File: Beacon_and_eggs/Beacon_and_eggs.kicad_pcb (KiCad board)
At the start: 4 copper layers, 40 x 70 mm, 71 parts, among them J1 USB_C_Receptacle_USB2.0_16P, J2 Conn_01x03_Pin, J3 Conn_01x02_Pin, Q1 NTA4151P, Q2 NTA4153N, SW3 RESET, SW4 BOOT0, U1 SA818V, U2 STM32F411CEUx, U3 ADXL343, U4 MIC5528-3.3YMX-TR, U6 BQ24070RHLR, Y1 25MHz 18pF, Y2 32.768kHz 12.5pF

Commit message: added missing via net labels
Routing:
- net GND: vias 44 -> 61
- net (no net): vias 17 -> 1
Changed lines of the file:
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@@
 	)
 	(via
-		(at 133 62)
-		(size 0.6)
-		(drill 0.3)
-		(layers "F.Cu" "B.Cu")
-		(net 0)
-	)
-	(via
-		(at 131 60)
-		(size 0.6)
-		(drill 0.3)
-		(layers "F.Cu" "B.Cu")
-		(net 0)
-	)
-	(via
-		(at 138 67)
-		(size 0.6)
-		(drill 0.3)
-		(layers "F.Cu" "B.Cu")
-		(net 0)
-	)
-	(via
-		(at 130 59)
-		(size 0.6)
-		(drill 0.3)
-		(layers "F.Cu" "B.Cu")
-		(net 0)
-	)
-	(via
-		(at 137 66)
-		(size 0.6)
-		(drill 0.3)
-		(layers "F.Cu" "B.Cu")
-		(net 0)
-	)
-	(via
-		(at 134 63)
-		(size 0.6)
-		(drill 0.3)
-		(layers "F.Cu" "B.Cu")
-		(net 0)
-	)
-	(via
-		(at 130 63)
-		(size 0.6)
-		(drill 0.3)
-		(layers "F.Cu" "B.Cu")
-		(net 0)
-	)
-	(via
-		(at 129 58)
-		(size 0.6)
-		(drill 0.3)
-		(layers "F.Cu" "B.Cu")
-		(net 0)
-	)
-	(via
-		(at 132 61)
-		(size 0.6)
-		(drill 0.3)
-		(layers "F.Cu" "B.Cu")
-		(net 0)
-	)
-	(via
-		(at 136 65)
-		(size 0.6)
-		(drill 0.3)
-		(layers "F.Cu" "B.Cu")
-		(net 0)
-	)
-	(via
-		(at 135 68)
-		(size 0.6)
-		(drill 0.3)
-		(layers "F.Cu" "B.Cu")
-		(net 0)
-	)
-	(via
-		(at 128 61)
-		(size 0.6)
-		(drill 0.3)
-		(layers "F.Cu" "B.Cu")
-		(net 0)
-	)
-	(via
-		(at 127 60)
-		(size 0.6)
-		(drill 0.3)
-		(layers "F.Cu" "B.Cu")
-		(net 0)
-	)
-	(via
-		(at 131 64)
-		(size 0.6)
-		(drill 0.3)
-		(layers "F.Cu" "B.Cu")
-		(net 0)
-	)
-	(via
-		(at 136 69)
-		(size 0.6)
-		(drill 0.3)
-		(layers "F.Cu" "B.Cu")
-		(net 0)
-	)
-	(via
-		(at 129 62)
-		(size 0.6)
-		(drill 0.3)
-		(layers "F.Cu" "B.Cu")
-		(net 0)
-	)
-	(via
-		(at 132 65)
+		(at 137.668 70.104)
 		(size 0.6)
 		(drill 0.3)
@@
 	)
 	(via
+		(at 133 62)
+		(size 0.6)
+		(drill 0.3)
+		(layers "F.Cu" "B.Cu")
+		(free yes)
+		(net 2)
+	)
+	(via
 		(at 153.5275 65.6075)
 		(size 0.6)
@@
 	)
 	(via
+		(at 131 60)
+		(size 0.6)
+		(drill 0.3)
+		(layers "F.Cu" "B.Cu")
+		(free yes)
+		(net 2)
+	)
+	(via
+		(at 138 67)
+		(size 0.6)
+		(drill 0.3)
+		(layers "F.Cu" "B.Cu")
+		(free yes)
+		(net 2)
+	)
+	(via
+		(at 130 59)
+		(size 0.6)
+		(drill 0.3)
+		(layers "F.Cu" "B.Cu")
+		(free yes)
+		(net 2)
+	)
+	(via
+		(at 137 66)
+		(size 0.6)
+		(drill 0.3)
+		(layers "F.Cu" "B.Cu")
+		(free yes)
+		(net 2)
+	)
+	(via
 		(at 151.8475 84)
 		(size 0.6)
@@
 	)
 	(via
+		(at 134 63)
+		(size 0.6)
+		(drill 0.3)
+		(layers "F.Cu" "B.Cu")
+		(free yes)
+		(net 2)
+	)
+	(via
 		(at 144.6 72.8)
 		(size 0.6)
@@
 	)
 	(via
+		(at 130 63)
+		(size 0.6)
+		(drill 0.3)
+		(layers "F.Cu" "B.Cu")
+		(free yes)
+		(net 2)
+	)
+	(via
+		(at 129 58)
+		(size 0.6)
+		(drill 0.3)
+		(layers "F.Cu" "B.Cu")
+		(free yes)
+		(net 2)
+	)
+	(via
 		(at 150.4025 70.3325)
 		(size 0.6)
@@
 	)
 	(via
+		(at 132 61)
+		(size 0.6)
+		(drill 0.3)
+		(layers "F.Cu" "B.Cu")
+		(free yes)
+		(net 2)
+	)
+	(via
 		(at 149.8 59.8)
 		(size 0.6)
@@
 	)
 	(via
+		(at 136 65)
+		(size 0.6)
+		(drill 0.3)
+		(layers "F.Cu" "B.Cu")
+		(free yes)
+		(net 2)
+	)
+	(via
 		(at 135.6 104.7)
 		(size 0.6)
@@
 	)
 	(via
+		(at 135 68)
+		(size 0.6)
+		(drill 0.3)
+		(layers "F.Cu" "B.Cu")
+		(free yes)
+		(net 2)
+	)
+	(via
 		(at 130.16 106.8)
 		(size 0.6)
@@
 	)
 	(via
+		(at 128 61)
+		(size 0.6)
+		(drill 0.3)
+		(layers "F.Cu" "B.Cu")
+		(free yes)
+		(net 2)
+	)
+	(via
 		(at 143.5675 97.16)
 		(size 0.6)
@@
 	)
 	(via
+		(at 127 60)
+		(size 0.6)
+		(drill 0.3)
+		(layers "F.Cu" "B.Cu")
+		(free yes)
+		(net 2)
+	)
+	(via
 		(at 140.07 108.47)
 		(size 0.6)
@@
 	)
 	(via
+		(at 131 64)
+		(size 0.6)
+		(drill 0.3)
+		(layers "F.Cu" "B.Cu")
+		(free yes)
+		(net 2)
+	)
+	(via
 		(at 122.5 60.75)
 		(size 0.6)
@@
 	)
 	(via
+		(at 136 69)
+		(size 0.6)
+		(drill 0.3)
+		(layers "F.Cu" "B.Cu")
+		(free yes)
+		(net 2)
+	)
+	(via
+		(at 129 62)
+		(size 0.6)
+		(drill 0.3)
+		(layers "F.Cu" "B.Cu")
+		(free yes)
+		(net 2)
+	)
+	(via
+		(at 132 65)
+		(size 0.6)
+		(drill 0.3)
+		(layers "F.Cu" "B.Cu")
+		(free yes)
+		(net 2)
+	)
+	(via
 		(at 146.349661 99.3225)
 		(size 0.6)
@@
 		(start 137.5706 68.525)
 		(end 140.225 68.525)
-		(width 0.2)
+		(width 0.3)
 		(layer "F.Cu")
 		(net 63)
@@
 		(start 125.0372 56)
 		(end 137.5664 68.5292)
-		(width 0.2)
+		(width 0.3)
 		(layer "B.Cu")
 		(net 63)
@@
 		(min_thickness 0.25)
 		(filled_areas_thickness no)
-		(fill yes
+		(fill
 			(thermal_gap 0.5)
 			(thermal_bridge_width 0.5)
@@
 		(min_thickness 0.25)
 		(filled_areas_thickness no)
-		(fill yes
+		(fill
 			(thermal_gap 0.5)
 			(thermal_bridge_width 0.5)
@@
 		(min_thickness 0.25)
 		(filled_areas_thickness no)
-		(fill yes
+		(fill
 			(thermal_gap 0.5)
 			(thermal_bridge_width 0.5)
@@
 		(min_thickness 0.25)
 		(filled_areas_thickness no)
-		(fill yes
+		(fill
 			(thermal_gap 0.5)
 			(thermal_bridge_width 0.5)
@@
 		(min_thickness 0.25)
 		(filled_areas_thickness no)
-		(fill yes
+		(fill
 			(thermal_gap 0.5)
 			(thermal_bridge_width 0.5)
@@
 		(min_thickness 0.25)
 		(filled_areas_thickness no)
-		(fill yes
+		(fill
 			(thermal_gap 0.5)
 			(thermal_bridge_width 0.5)

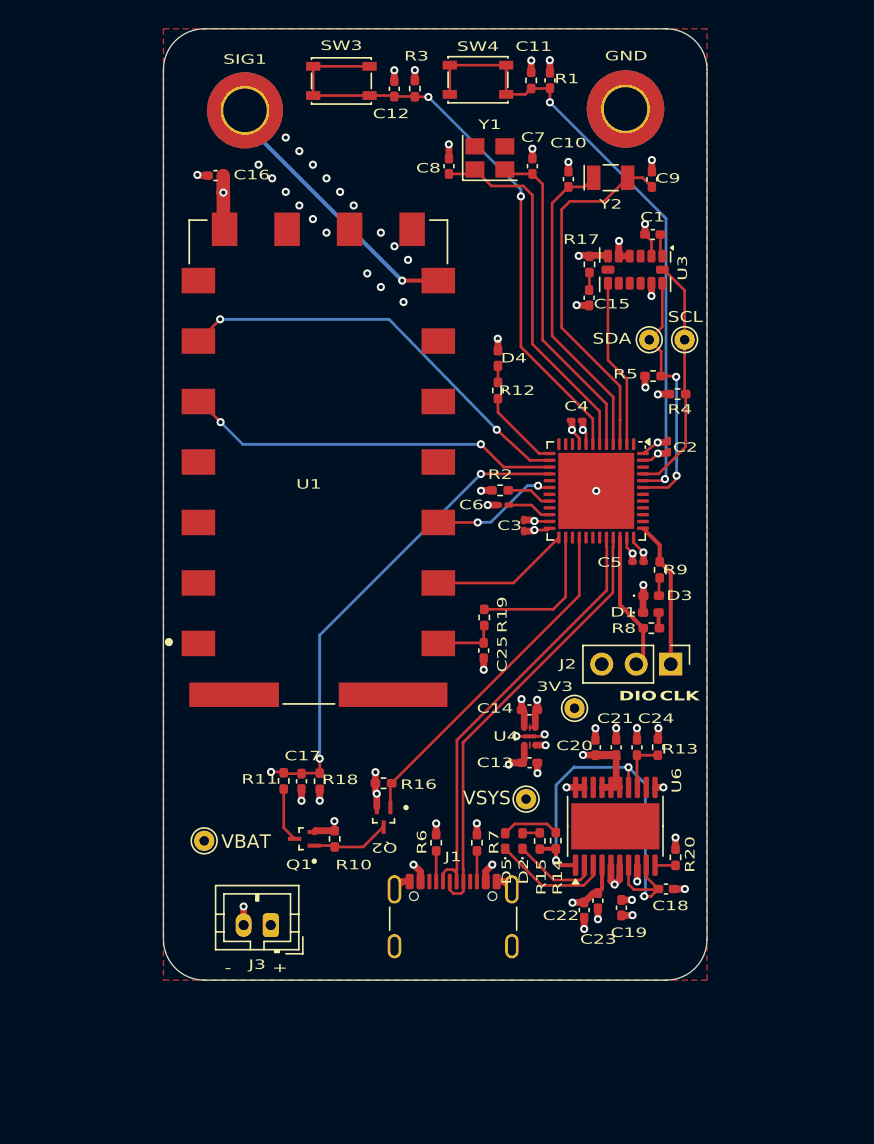
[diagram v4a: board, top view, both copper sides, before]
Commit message: Added complete BOM, replaced a footprint, added missing STEP files
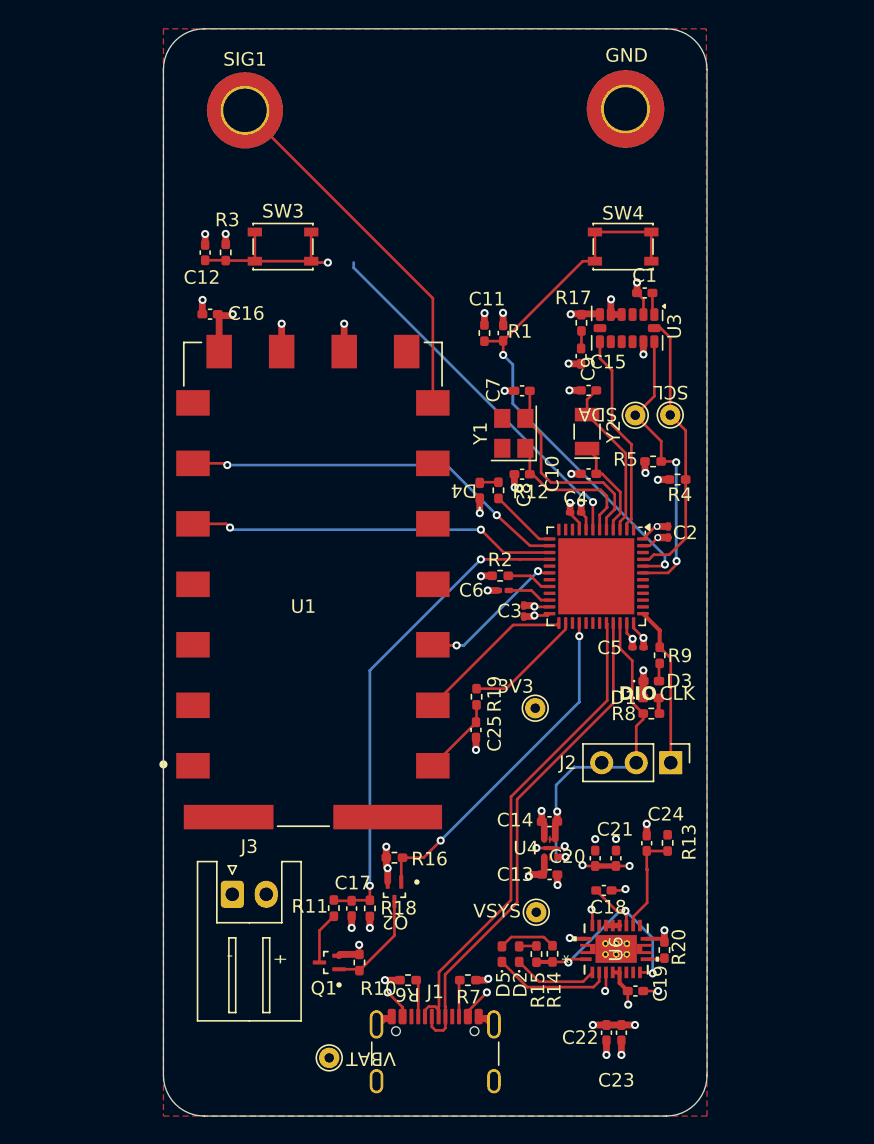
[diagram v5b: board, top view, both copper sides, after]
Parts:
- C1: value 0.1F -> 0.1uF
- C11, C12: value 0.1uf -> 0.1uF
- J3: footprint Connector_JST:JST_PH_B2B-PH-K_1x02_P2.00mm_Vertical -> Connector_JST:JST_XH_S2B-XH-A_1x02_P2.50mm_Horizontal
- U1: value SA818V -> SA868S
- U2: value STM32F411CEUx -> STM32F411CEU6TR
- U6: footprint Package_SO:HTSSOP-20-1EP_4.4x6.5mm_P0.65mm_EP3.4x6.5mm_Mask2.4x3.7mm -> BQ24070RHLR:RHL20_2P05X3P05
- moved C8 23.3 mm to (146.4, 82.8), turned to 0 degrees
- moved C10 21.7 mm to (151.3, 82.7), turned to 0 degrees
- moved Y1 20.3 mm to (145.8, 79.8), turned to 90 degrees
- moved C11 18.9 mm to (145.0, 72.4)
- moved R1 18.9 mm to (143.6, 72.4)
- moved Y2 18.8 mm to (151.2, 79.6), turned to 90 degrees
- moved TP5 18.4 mm to (132.2, 125.7)
- moved C12 18.4 mm to (123.1, 66.5)
- moved R3 18.4 mm to (124.6, 66.5)
- moved C7 16.5 mm to (146.4, 76.6), turned to 0 degrees
- moved SW4 16.3 mm to (153.8, 66.0)
- moved C9 16.2 mm to (151.3, 76.6), turned to 0 degrees
- moved SW3 12.9 mm to (128.8, 66.0)
- moved R6 10.3 mm to (138.0, 120.0), turned to 180 degrees
- moved C16 10.2 mm to (123.4, 71.0)
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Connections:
- U6 pad 21: GND -> unconnected-(U6-EPAD-Pad21)
- U6 pad 7: /VREF -> unconnected-(U6-ISET2-Pad7)
- U6 pad 8: GND -> unconnected-(U6-MODE-Pad8)
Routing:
- net /X1_OUT: track 27.4 -> 11.1 mm
- net /X2_OUT: track 23.4 -> 7.44 mm
- net /X2_IN: track 26.9 -> 11.9 mm
- net /VREF: track 34.0 -> 20.0 mm
- net GND: track 52.6 -> 66.4 mm, vias 61 -> 42
- net /X1_IN: track 24.3 -> 15.5 mm
- net /ANT_SIG: track 21.1 -> 27.3 mm, vias 1 -> 0
- net /NRST: track 45.9 -> 40.8 mm
- net /USB_DN: track 32.7 -> 37.0 mm
- net /USB_DP: track 32.7 -> 37.1 mm
- net /BOOT0: track 46.1 -> 42.2 mm
- net Net-(U6-DPPM): track 3.93 -> 7.61 mm
- net /SDA: track 19.1 -> 21.7 mm
- net VSYS: track 13.8 -> 11.2 mm, vias 4 -> 5
- net /ACCEL_INT1: track 12.4 -> 15.0 mm
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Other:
- board size 40 x 70 mm -> 40 x 80 mm

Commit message: edited silkscreen text
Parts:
- moved TP6 1.38 mm to (148.8, 114.9)
- moved 3V3 0.78 mm to (148.0, 99.5)
- moved C18 0.49 mm to (152.4, 113.9)
- renumbered SW4 to BOOT0, SW3 to RST
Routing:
- net GND: vias 42 -> 44
